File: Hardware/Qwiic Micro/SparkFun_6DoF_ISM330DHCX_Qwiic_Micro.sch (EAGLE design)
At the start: 23 parts, among them J1 Qwiic Right Angle, U1 ISM330DHCX

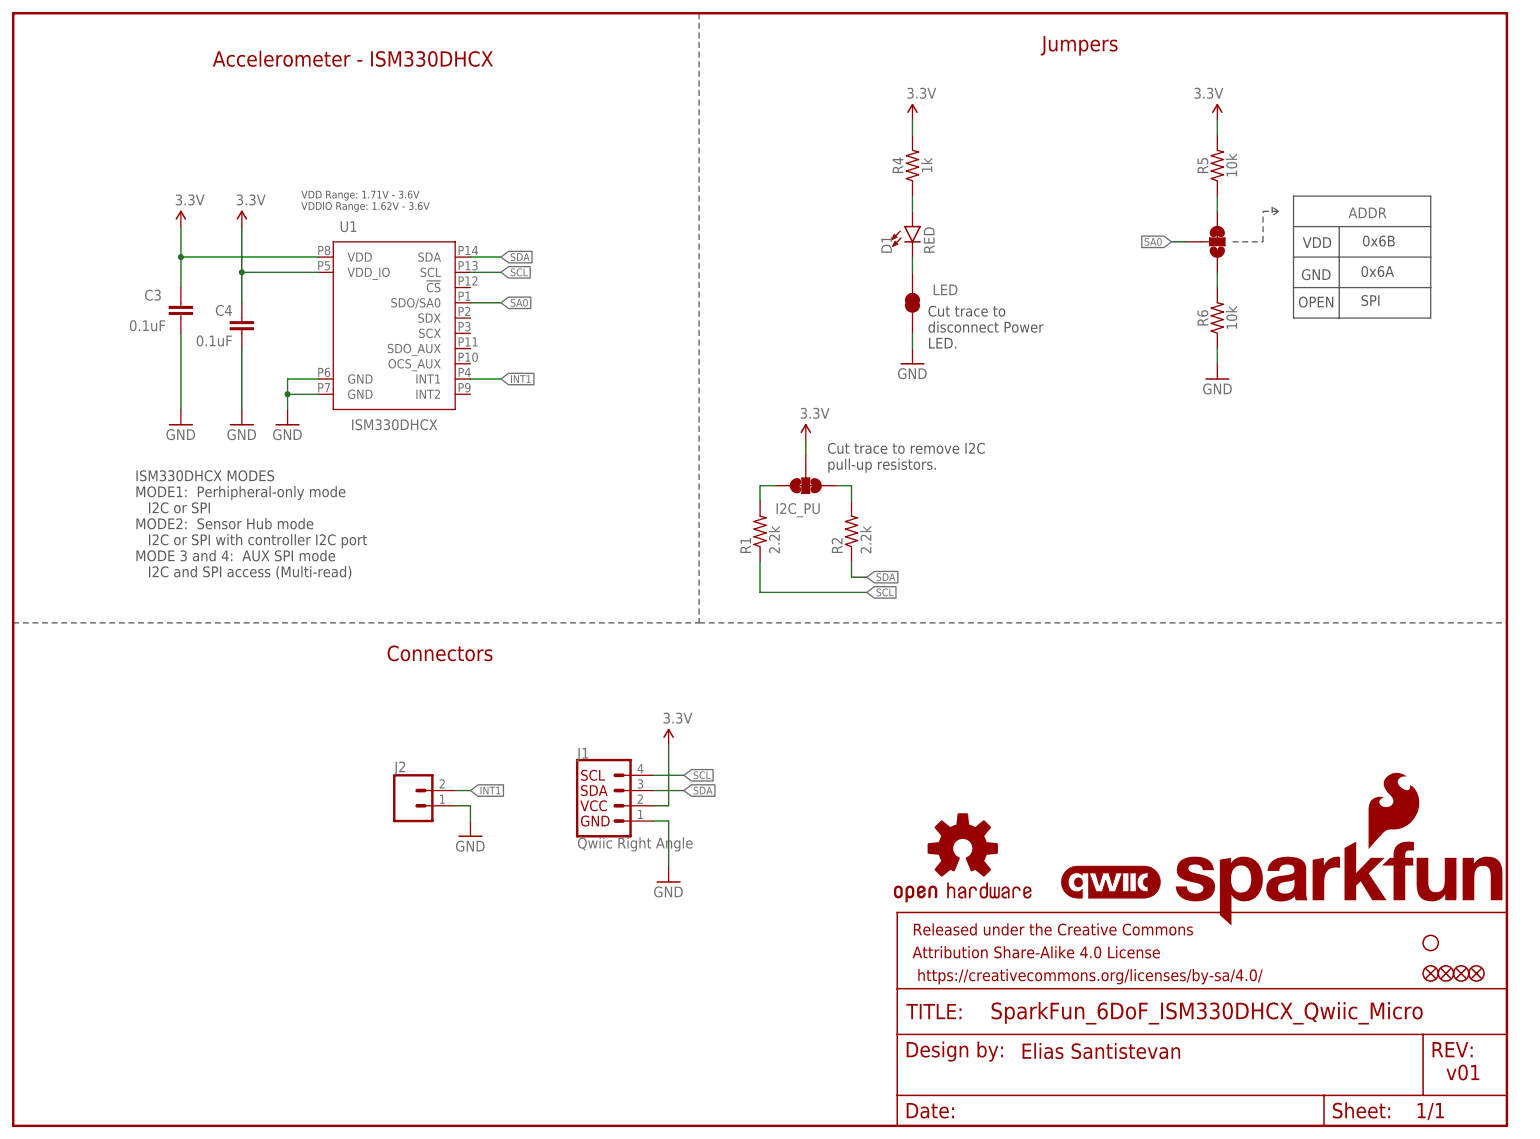
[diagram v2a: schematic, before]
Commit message: Extends board to 0.75", adds better labels, adds 0402 LED to design
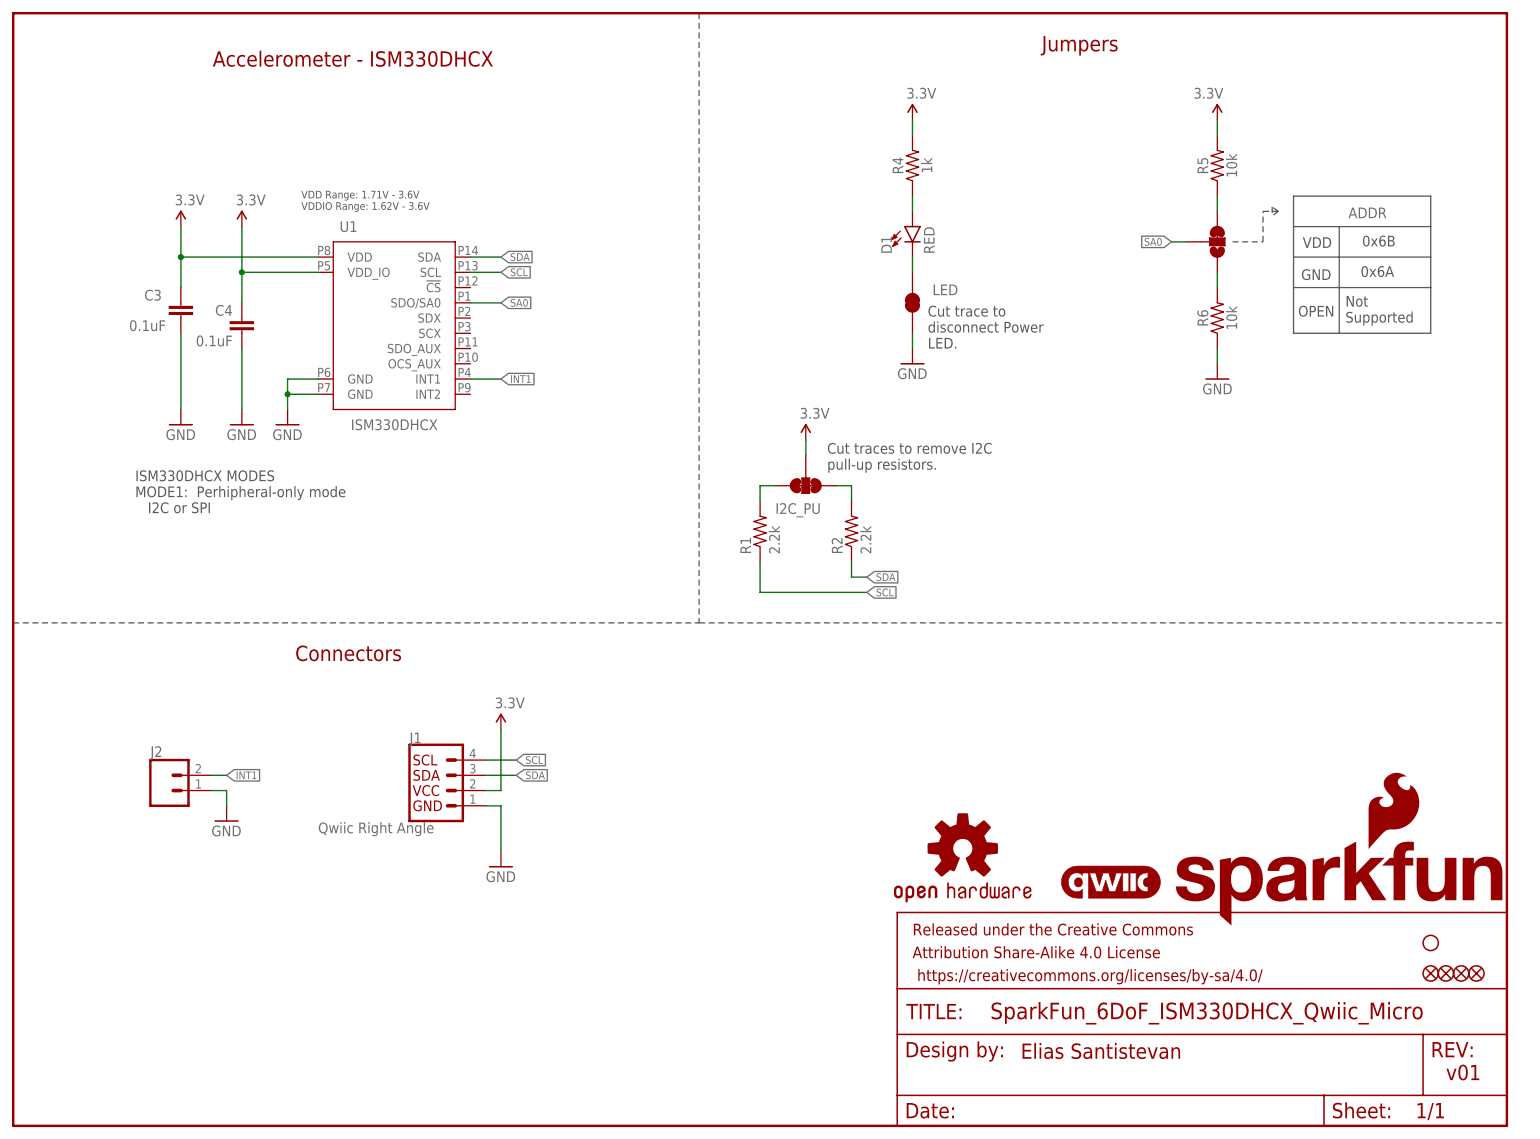
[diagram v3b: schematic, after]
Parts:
- D1: device SparkFun-LED:LED-RED0603 -> ISM330DHCX:LED_0402
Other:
- note added: "Cut traces to remove I2C pull-up resistors."
- note added: "ISM330DHCX MODES MODE1: Perhipheral-only mode I2C or SPI"
- note added: "Not Supported"
- note removed: "Cut trace to remove I2C pull-up resistors."
- note removed: "ISM330DHCX MODES MODE1: Perhipheral-only mode I2C or SPI MODE2: Sensor Hub mode I2C or SPI with controller I2C port MODE 3 and 4: AUX SPI mode I2C and SPI access (Multi-read)"
- note removed: "SPI"
- moved on the sheet: J1, J2
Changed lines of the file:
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@@
 <part name="FD1" library="SparkFun-Aesthetics" deviceset="FIDUCIAL" device="UFIDUCIAL"/>
 <part name="FD2" library="SparkFun-Aesthetics" deviceset="FIDUCIAL" device="UFIDUCIAL"/>
-<part name="D1" library="SparkFun-LED" deviceset="LED-RED" device="0603" value="RED"/>
+<part name="D1" library="ISM330DHCX" deviceset="LED_0402" device="" value="RED"/>
 <part name="R4" library="SparkFun-Resistors" deviceset="1KOHM" device="-0402T-1/16W-1%" value="1k"/>
 <part name="LED" library="SparkFun-Jumpers" deviceset="JUMPER-SMT_2_NC_TRACE" device="_SILK" package3d_urn="urn:adsk.eagle:package:39281/1"/>
@@
 <plain>
 <text x="56.642" y="177.8" size="2.54" layer="94" font="vector" align="center">Accelerometer - ISM330DHCX</text>
-<text x="135.636" y="113.792" size="1.778" layer="97" font="vector" align="top-left">Cut trace to remove I2C
+<text x="135.636" y="113.792" size="1.778" layer="97" font="vector" align="top-left">Cut traces to remove I2C
 pull-up resistors.</text>
 <text x="20.32" y="109.22" size="1.778" layer="97" font="vector" align="top-left">ISM330DHCX MODES
 MODE1:  Perhipheral-only mode
    I2C or SPI
-MODE2:  Sensor Hub mode
-   I2C or SPI with controller I2C port
-MODE 3 and 4:  AUX SPI mode
-   I2C and SPI access (Multi-read)   </text>
+</text>
 <wire x1="0" y1="83.82" x2="114.3" y2="83.82" width="0.2032" layer="97" style="longdash"/>
 <wire x1="114.3" y1="83.82" x2="248.92" y2="83.82" width="0.2032" layer="97" style="longdash"/>
@@
 disconnect Power
 LED.</text>
-<text x="71.12" y="78.74" size="2.54" layer="94" font="vector" align="center">Connectors</text>
+<text x="55.88" y="78.74" size="2.54" layer="94" font="vector" align="center">Connectors</text>
 <wire x1="213.36" y1="154.94" x2="213.36" y2="149.86" width="0.2032" layer="97"/>
 <wire x1="213.36" y1="149.86" x2="213.36" y2="144.78" width="0.2032" layer="97"/>
 <wire x1="213.36" y1="144.78" x2="213.36" y2="139.7" width="0.2032" layer="97"/>
-<wire x1="213.36" y1="139.7" x2="213.36" y2="134.62" width="0.2032" layer="97"/>
-<wire x1="213.36" y1="134.62" x2="220.98" y2="134.62" width="0.2032" layer="97"/>
-<wire x1="220.98" y1="134.62" x2="236.22" y2="134.62" width="0.2032" layer="97"/>
-<wire x1="236.22" y1="134.62" x2="236.22" y2="139.7" width="0.2032" layer="97"/>
+<wire x1="213.36" y1="139.7" x2="213.36" y2="132.08" width="0.2032" layer="97"/>
+<wire x1="213.36" y1="132.08" x2="220.98" y2="132.08" width="0.2032" layer="97"/>
+<wire x1="220.98" y1="132.08" x2="236.22" y2="132.08" width="0.2032" layer="97"/>
+<wire x1="236.22" y1="132.08" x2="236.22" y2="139.7" width="0.2032" layer="97"/>
 <wire x1="236.22" y1="139.7" x2="236.22" y2="144.78" width="0.2032" layer="97"/>
 <wire x1="236.22" y1="144.78" x2="236.22" y2="149.86" width="0.2032" layer="97"/>
@@
 <wire x1="220.98" y1="149.86" x2="220.98" y2="144.78" width="0.2032" layer="97"/>
 <wire x1="220.98" y1="144.78" x2="220.98" y2="139.7" width="0.2032" layer="97"/>
-<wire x1="220.98" y1="139.7" x2="220.98" y2="134.62" width="0.2032" layer="97"/>
+<wire x1="220.98" y1="139.7" x2="220.98" y2="132.08" width="0.2032" layer="97"/>
 <wire x1="220.98" y1="144.78" x2="236.22" y2="144.78" width="0.2032" layer="97"/>
 <wire x1="220.98" y1="139.7" x2="236.22" y2="139.7" width="0.2032" layer="97"/>
@@
 <text x="214.884" y="146.304" size="1.778" layer="97" font="vector">VDD</text>
 <text x="214.63" y="140.97" size="1.778" layer="97" font="vector">GND</text>
-<text x="214.122" y="136.398" size="1.778" layer="97" font="vector">OPEN</text>
+<text x="214.122" y="134.874" size="1.778" layer="97" font="vector">OPEN</text>
 <text x="224.79" y="146.558" size="1.778" layer="97" font="vector">0x6B</text>
 <text x="224.536" y="141.478" size="1.778" layer="97" font="vector">0x6A</text>
-<text x="224.536" y="136.652" size="1.778" layer="97" font="vector">SPI</text>
 <wire x1="203.2" y1="147.32" x2="208.28" y2="147.32" width="0.2032" layer="97" style="dashdot"/>
 <wire x1="208.28" y1="147.32" x2="208.28" y2="152.4" width="0.2032" layer="97" style="dashdot"/>
@@
 <wire x1="210.82" y1="152.4" x2="209.804" y2="151.638" width="0.2032" layer="97" style="dashdot"/>
 <text x="167.894" y="11.176" size="2.54" layer="94" font="vector">Elias Santistevan</text>
+<text x="221.996" y="133.858" size="1.778" layer="97" font="vector">Not
+Supported</text>
 </plain>
 <instances>
@@
 <attribute name="VALUE" x="202.184" y="134.62" size="1.778" layer="96" font="vector" rot="R90" align="top-center"/>
 </instance>
-<instance part="J1" gate="G$1" x="99.06" y="53.34" smashed="yes">
-<attribute name="VALUE" x="93.98" y="48.006" size="1.778" layer="96" font="vector" align="top-left"/>
-<attribute name="NAME" x="93.98" y="61.214" size="1.778" layer="95" font="vector"/>
-</instance>
-<instance part="GND3" gate="1" x="109.22" y="40.64" smashed="yes">
-<attribute name="VALUE" x="106.68" y="38.1" size="1.778" layer="96" font="vector"/>
-</instance>
-<instance part="SUPPLY1" gate="G$1" x="109.22" y="63.5" smashed="yes">
-<attribute name="VALUE" x="108.204" y="67.056" size="1.778" layer="96" font="vector"/>
+<instance part="J1" gate="G$1" x="71.12" y="55.88" smashed="yes">
+<attribute name="VALUE" x="50.8" y="50.546" size="1.778" layer="96" font="vector" align="top-left"/>
+<attribute name="NAME" x="66.04" y="63.754" size="1.778" layer="95" font="vector"/>
+</instance>
+<instance part="GND3" gate="1" x="81.28" y="43.18" smashed="yes">
+<attribute name="VALUE" x="78.74" y="40.64" size="1.778" layer="96" font="vector"/>
+</instance>
+<instance part="SUPPLY1" gate="G$1" x="81.28" y="66.04" smashed="yes">
+<attribute name="VALUE" x="80.264" y="69.596" size="1.778" layer="96" font="vector"/>
 </instance>
 <instance part="LOGO1" gate="G$1" x="182.88" y="40.64" smashed="yes"/>
 <instance part="LOGO3" gate="G$1" x="193.04" y="33.02" smashed="yes"/>
-<instance part="J2" gate="G$1" x="66.04" y="53.34" smashed="yes">
-<attribute name="VALUE" x="63.5" y="48.514" size="1.778" layer="96" font="vector"/>
-<attribute name="NAME" x="63.5" y="58.928" size="1.778" layer="95" font="vector"/>
-</instance>
-<instance part="GND1" gate="1" x="76.2" y="48.26" smashed="yes">
-<attribute name="VALUE" x="73.66" y="45.72" size="1.778" layer="96" font="vector"/>
+<instance part="J2" gate="G$1" x="25.4" y="55.88" smashed="yes">
+<attribute name="VALUE" x="22.86" y="51.054" size="1.778" layer="96" font="vector"/>
+<attribute name="NAME" x="22.86" y="61.468" size="1.778" layer="95" font="vector"/>
+</instance>
+<instance part="GND1" gate="1" x="35.56" y="50.8" smashed="yes">
+<attribute name="VALUE" x="33.02" y="48.26" size="1.778" layer="96" font="vector"/>
 </instance>
 </instances>
@@
 <segment>
 <pinref part="J1" gate="G$1" pin="1"/>
-<wire x1="106.68" y1="50.8" x2="109.22" y2="50.8" width="0.1524" layer="91"/>
-<wire x1="109.22" y1="50.8" x2="109.22" y2="43.18" width="0.1524" layer="91"/>
+<wire x1="78.74" y1="53.34" x2="81.28" y2="53.34" width="0.1524" layer="91"/>
+<wire x1="81.28" y1="53.34" x2="81.28" y2="45.72" width="0.1524" layer="91"/>
 <pinref part="GND3" gate="1" pin="GND"/>
 </segment>
 <segment>
 <pinref part="J2" gate="G$1" pin="1"/>
-<wire x1="73.66" y1="53.34" x2="76.2" y2="53.34" width="0.1524" layer="91"/>
-<wire x1="76.2" y1="53.34" x2="76.2" y2="50.8" width="0.1524" layer="91"/>
+<wire x1="33.02" y1="55.88" x2="35.56" y2="55.88" width="0.1524" layer="91"/>
+<wire x1="35.56" y1="55.88" x2="35.56" y2="53.34" width="0.1524" layer="91"/>
 <pinref part="GND1" gate="1" pin="GND"/>
 </segment>
@@
 <segment>
 <pinref part="J1" gate="G$1" pin="4"/>
-<wire x1="106.68" y1="58.42" x2="111.76" y2="58.42" width="0.1524" layer="91"/>
-<label x="111.76" y="58.42" size="1.27" layer="95" font="vector" xref="yes"/>
+<wire x1="78.74" y1="60.96" x2="83.82" y2="60.96" width="0.1524" layer="91"/>
+<label x="83.82" y="60.96" size="1.27" layer="95" font="vector" xref="yes"/>
 </segment>
 </net>
@@
 <segment>
 <pinref part="J1" gate="G$1" pin="3"/>
-<wire x1="106.68" y1="55.88" x2="111.76" y2="55.88" width="0.1524" layer="91"/>
-<label x="111.76" y="55.88" size="1.27" layer="95" font="vector" xref="yes"/>
+<wire x1="78.74" y1="58.42" x2="83.82" y2="58.42" width="0.1524" layer="91"/>
+<label x="83.82" y="58.42" size="1.27" layer="95" font="vector" xref="yes"/>
 </segment>
 </net>
@@
 </segment>
 <segment>
-<wire x1="73.66" y1="55.88" x2="76.2" y2="55.88" width="0.1524" layer="91"/>
-<label x="76.2" y="55.88" size="1.27" layer="95" font="vector" xref="yes"/>
+<wire x1="33.02" y1="58.42" x2="35.56" y2="58.42" width="0.1524" layer="91"/>
+<label x="35.56" y="58.42" size="1.27" layer="95" font="vector" xref="yes"/>
 <pinref part="J2" gate="G$1" pin="2"/>
 </segment>
@@
 <segment>
 <pinref part="J1" gate="G$1" pin="2"/>
-<wire x1="106.68" y1="53.34" x2="109.22" y2="53.34" width="0.1524" layer="91"/>
-<wire x1="109.22" y1="53.34" x2="109.22" y2="63.5" width="0.1524" layer="91"/>
+<wire x1="78.74" y1="55.88" x2="81.28" y2="55.88" width="0.1524" layer="91"/>
+<wire x1="81.28" y1="55.88" x2="81.28" y2="66.04" width="0.1524" layer="91"/>
 <pinref part="SUPPLY1" gate="G$1" pin="3.3V"/>
 </segment>

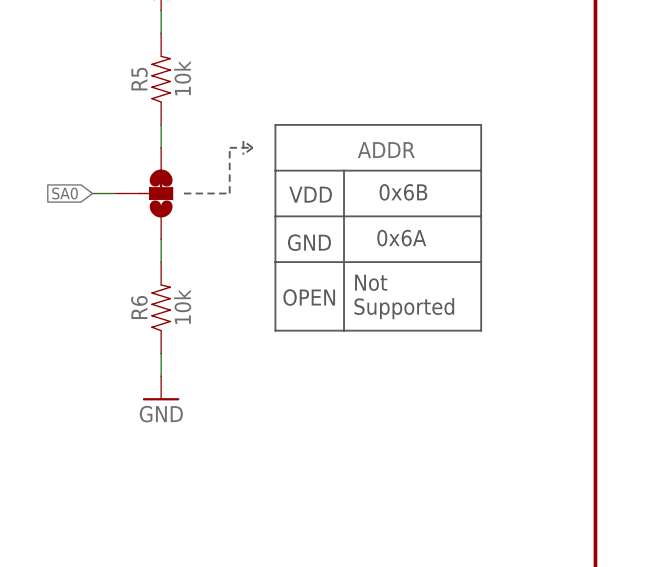
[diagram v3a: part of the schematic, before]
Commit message: Moves resistor so that PWR silk is close to the LED
* Fixes some trace bends
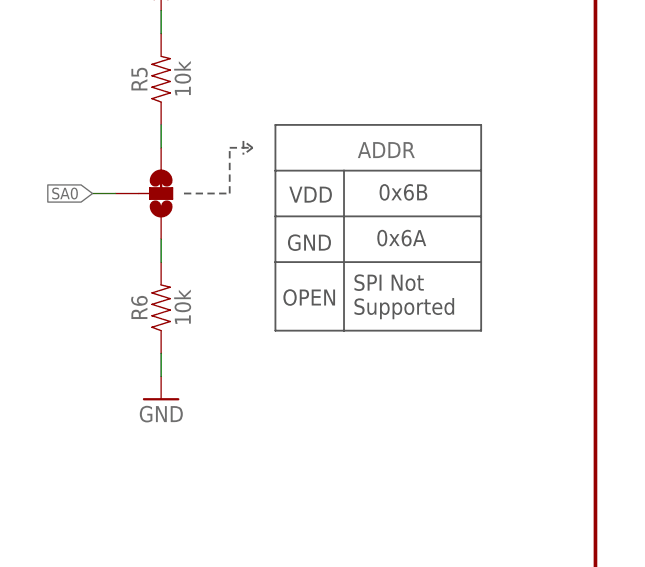
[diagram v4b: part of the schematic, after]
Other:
- note added: "SPI Not Supported"
- note removed: "Not Supported"
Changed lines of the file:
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@@
 <wire x1="210.82" y1="152.4" x2="209.804" y2="151.638" width="0.2032" layer="97" style="dashdot"/>
 <text x="167.894" y="11.176" size="2.54" layer="94" font="vector">Elias Santistevan</text>
-<text x="221.996" y="133.858" size="1.778" layer="97" font="vector">Not
+<text x="221.996" y="133.858" size="1.778" layer="97" font="vector">SPI Not
 Supported</text>
 </plain>
